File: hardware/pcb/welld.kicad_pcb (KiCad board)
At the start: 2 copper layers, 80 x 55 mm, 98 parts, among them J1 LiPo, J10 PROG, J12 Solar, J2 USB-C, J3 U.FL, J4 4-20mA_1, J5 4-20mA_2, J6 DS18B20, J7 Spare, J8 I2C, J9 GPIO, Q1 BSS123, Q2 BSS123, SW1 RESET, SW2 BOOT, U1 TPS7A0533, U10 MAX17048, U2 TP4056, U3 S-8261A, U4 FS8205A, U5 USBLC6, U6 ESP32-C6, U7 CN3791, U8 TPS61023, U9 ADS1115

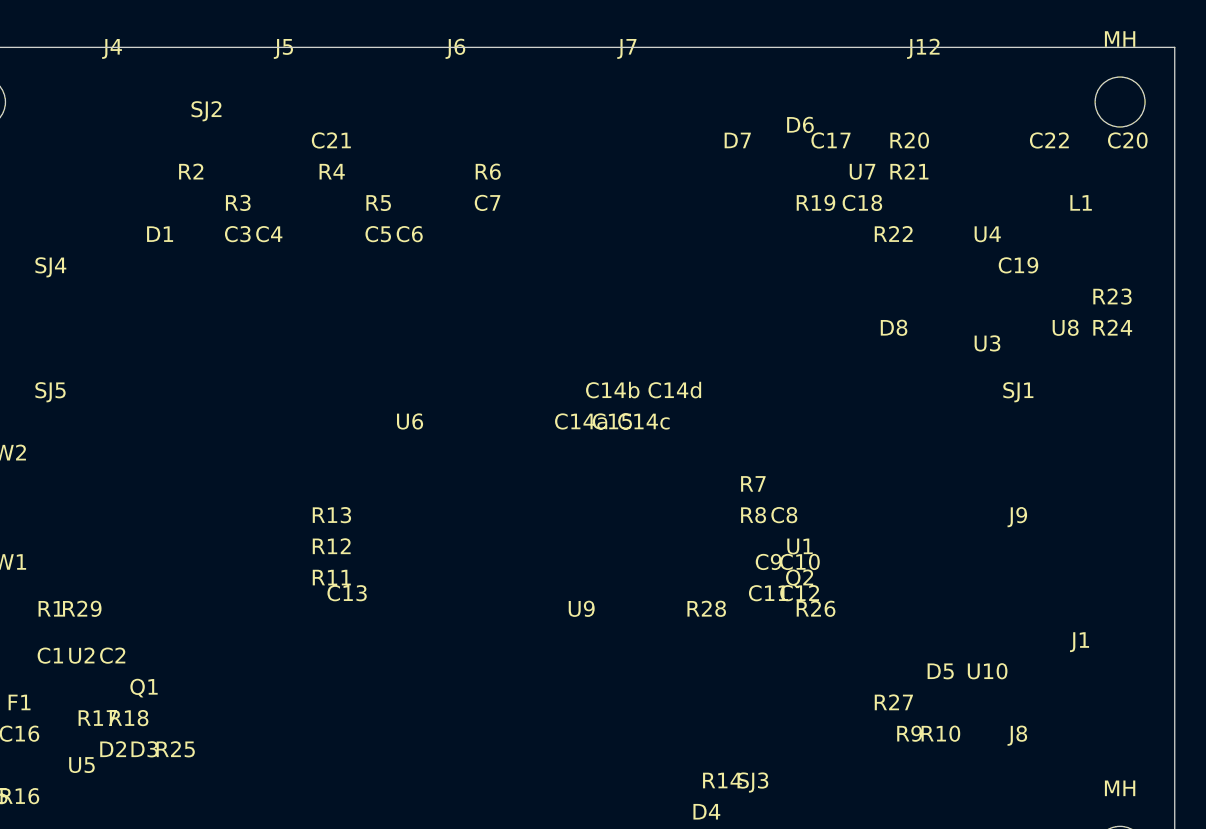
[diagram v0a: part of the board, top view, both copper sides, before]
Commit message: PCB analog/protection/interlock fixes + three new agents
Analog front-end:
- C3, C5: 100nF → 1µF to lower RC filter corner from 15.9kHz to 1.6kHz
- Add FB1 (BLM18KG601SN1D ferrite) + C23/C24 (ADS1115 VDD bypass) to isolate
  the 16-bit ADC supply from TPS61023 switching noise and 2.4GHz radio

Transient protection:
- Add D9/D10 (SMAJ5.0CA, bidirectional, 400W) at J4/J5 SIG terminals before
  the shunt resistors — IEC 61000-4-5 surge protection for well-head cables
- Add D11 (SMAJ13A, 13V standoff, 400W) on VLOOP rail between U8 and field
  terminals to clamp cable back-EMF and lightning-induced transients

Charger interlock:
- Fix GPIO6 polarity throughout: CN3791 CHRG is active-LOW (was documented
  as active-high in CLAUDE.md and design.md GPIO table)
- Fix design.md: CN3791 has no EN/shutdown pin; GPIO6 reads CHRG output only
- Add Q3 (BSS84 P-ch) hardware interlock: gate=/CHRG_SOLAR, source=CE node,
  drain=GND; eliminates the boot-window race without firmware involvement
- Add R30 (10kΩ) as Q3 gate pull-up to +3V3

Agents:
- Add test-engineer, docs-writer, ci-engineer agents to .claude/agents/
- Expand CLAUDE.md Sub-Agent Routing Rules with full responsibility table
  and handoff order for hardware vs firmware-only changes

Co-Authored-By: Claude Sonnet 4.6 <noreply@anthropic.com>
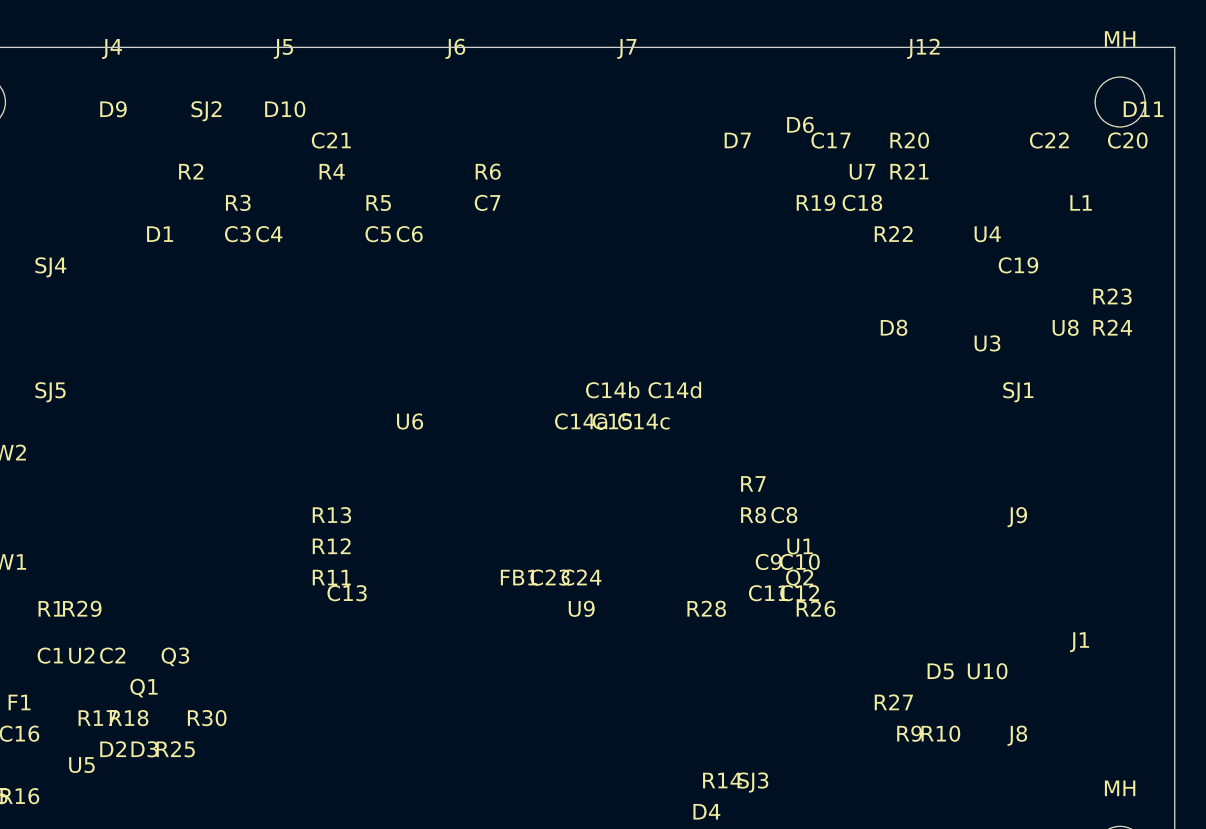
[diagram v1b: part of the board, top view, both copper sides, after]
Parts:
- added C23: 100nF, Capacitor_SMD:C_0402_1005Metric, F.Cu at (40.0, 36.0)
- added C24: 1uF, Capacitor_SMD:C_0402_1005Metric, F.Cu at (42.0, 36.0)
- added D10: SMAJ5.0CA, Diode_SMD:D_SMA, F.Cu at (23.0, 6.00)
- added D11: SMAJ13A, Diode_SMD:D_SMA, F.Cu at (78.0, 6.00)
- added D9: SMAJ5.0CA, Diode_SMD:D_SMA, F.Cu at (12.0, 6.00)
- added FB1: 600R@100MHz, Ferrite_Bead_SMD:L_0402_1005Metric, F.Cu at (38.0, 36.0)
- added Q3: BSS84, Package_TO_SOT_SMD:SOT-23, F.Cu at (16.0, 41.0)
- added R30: 10k, Resistor_SMD:R_0402_1005Metric, F.Cu at (18.0, 45.0)
- C3, C5: value 100nF -> 1uF
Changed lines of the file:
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@@
   (title_block
     (title "WellD Well-Level Monitor PCB")
-    (date "2026-05-16")
+    (date "2026-05-18")
     (company "WellD Project")
   )
@@
   (net 29 "ADS_DRDY")
   (net 30 "MAX_ALRT")
+  (net 31 "LOOP_TERM_CH1")
+  (net 32 "LOOP_TERM_CH2")
+  (net 33 "+3V3_ADS")
   (gr_line (start 0.000 0.000) (end 80.000 0.000)
     (stroke (width 0.05) (type solid)) (layer "Edge.Cuts")
@@
     )
   )
+  (footprint "Diode_SMD:D_SMA" (layer "F.Cu") (at 12.000 6.000 0.0)
+    (property "Reference" "D9" (at 0 -2 0) (layer "F.SilkS")
+      (effects (font (size 1 1) (thickness 0.15)))
+    )
+    (property "Value" "SMAJ5.0CA" (at 0 2 0) (layer "F.Fab")
+      (effects (font (size 1 1) (thickness 0.15)))
+    )
+  )
+  (footprint "Diode_SMD:D_SMA" (layer "F.Cu") (at 23.000 6.000 0.0)
+    (property "Reference" "D10" (at 0 -2 0) (layer "F.SilkS")
+      (effects (font (size 1 1) (thickness 0.15)))
+    )
+    (property "Value" "SMAJ5.0CA" (at 0 2 0) (layer "F.Fab")
+      (effects (font (size 1 1) (thickness 0.15)))
+    )
+  )
+  (footprint "Diode_SMD:D_SMA" (layer "F.Cu") (at 78.000 6.000 0.0)
+    (property "Reference" "D11" (at 0 -2 0) (layer "F.SilkS")
+      (effects (font (size 1 1) (thickness 0.15)))
+    )
+    (property "Value" "SMAJ13A" (at 0 2 0) (layer "F.Fab")
+      (effects (font (size 1 1) (thickness 0.15)))
+    )
+  )
   (footprint "LED_SMD:LED_0603_1608Metric" (layer "F.Cu") (at 12.000 47.000 0.0)
     (property "Reference" "D2" (at 0 -2 0) (layer "F.SilkS")
@@
       (effects (font (size 1 1) (thickness 0.15)))
     )
-    (property "Value" "100nF" (at 0 2 0) (layer "F.Fab")
+    (property "Value" "1uF" (at 0 2 0) (layer "F.Fab")
       (effects (font (size 1 1) (thickness 0.15)))
     )
@@
       (effects (font (size 1 1) (thickness 0.15)))
     )
-    (property "Value" "100nF" (at 0 2 0) (layer "F.Fab")
+    (property "Value" "1uF" (at 0 2 0) (layer "F.Fab")
       (effects (font (size 1 1) (thickness 0.15)))
     )
@@
     )
   )
+  (footprint "Ferrite_Bead_SMD:L_0402_1005Metric" (layer "F.Cu") (at 38.000 36.000 0.0)
+    (property "Reference" "FB1" (at 0 -2 0) (layer "F.SilkS")
+      (effects (font (size 1 1) (thickness 0.15)))
+    )
+    (property "Value" "600R@100MHz" (at 0 2 0) (layer "F.Fab")
+      (effects (font (size 1 1) (thickness 0.15)))
+    )
+  )
+  (footprint "Capacitor_SMD:C_0402_1005Metric" (layer "F.Cu") (at 40.000 36.000 0.0)
+    (property "Reference" "C23" (at 0 -2 0) (layer "F.SilkS")
+      (effects (font (size 1 1) (thickness 0.15)))
+    )
+    (property "Value" "100nF" (at 0 2 0) (layer "F.Fab")
+      (effects (font (size 1 1) (thickness 0.15)))
+    )
+  )
+  (footprint "Capacitor_SMD:C_0402_1005Metric" (layer "F.Cu") (at 42.000 36.000 0.0)
+    (property "Reference" "C24" (at 0 -2 0) (layer "F.SilkS")
+      (effects (font (size 1 1) (thickness 0.15)))
+    )
+    (property "Value" "1uF" (at 0 2 0) (layer "F.Fab")
+      (effects (font (size 1 1) (thickness 0.15)))
+    )
+  )
   (footprint "Package_SO:MSOP-10_3x3mm_P0.5mm" (layer "F.Cu") (at 42.000 38.000 0.0)
     (property "Reference" "U9" (at 0 -2 0) (layer "F.SilkS")
@@
     )
   )
+  (footprint "Package_TO_SOT_SMD:SOT-23" (layer "F.Cu") (at 16.000 41.000 0.0)
+    (property "Reference" "Q3" (at 0 -2 0) (layer "F.SilkS")
+      (effects (font (size 1 1) (thickness 0.15)))
+    )
+    (property "Value" "BSS84" (at 0 2 0) (layer "F.Fab")
+      (effects (font (size 1 1) (thickness 0.15)))
+    )
+  )
   (footprint "Resistor_SMD:R_0402_1005Metric" (layer "F.Cu") (at 16.000 47.000 0.0)
     (property "Reference" "R25" (at 0 -2 0) (layer "F.SilkS")
@@
       (effects (font (size 1 1) (thickness 0.15)))
     )
+  )
+  (footprint "Resistor_SMD:R_0402_1005Metric" (layer "F.Cu") (at 18.000 45.000 0.0)
+    (property "Reference" "R30" (at 0 -2 0) (layer "F.SilkS")
+      (effects (font (size 1 1) (thickness 0.15)))
+    )
+    (property "Value" "10k" (at 0 2 0) (layer "F.Fab")
+      (effects (font (size 1 1) (thickness 0.15)))
+    )

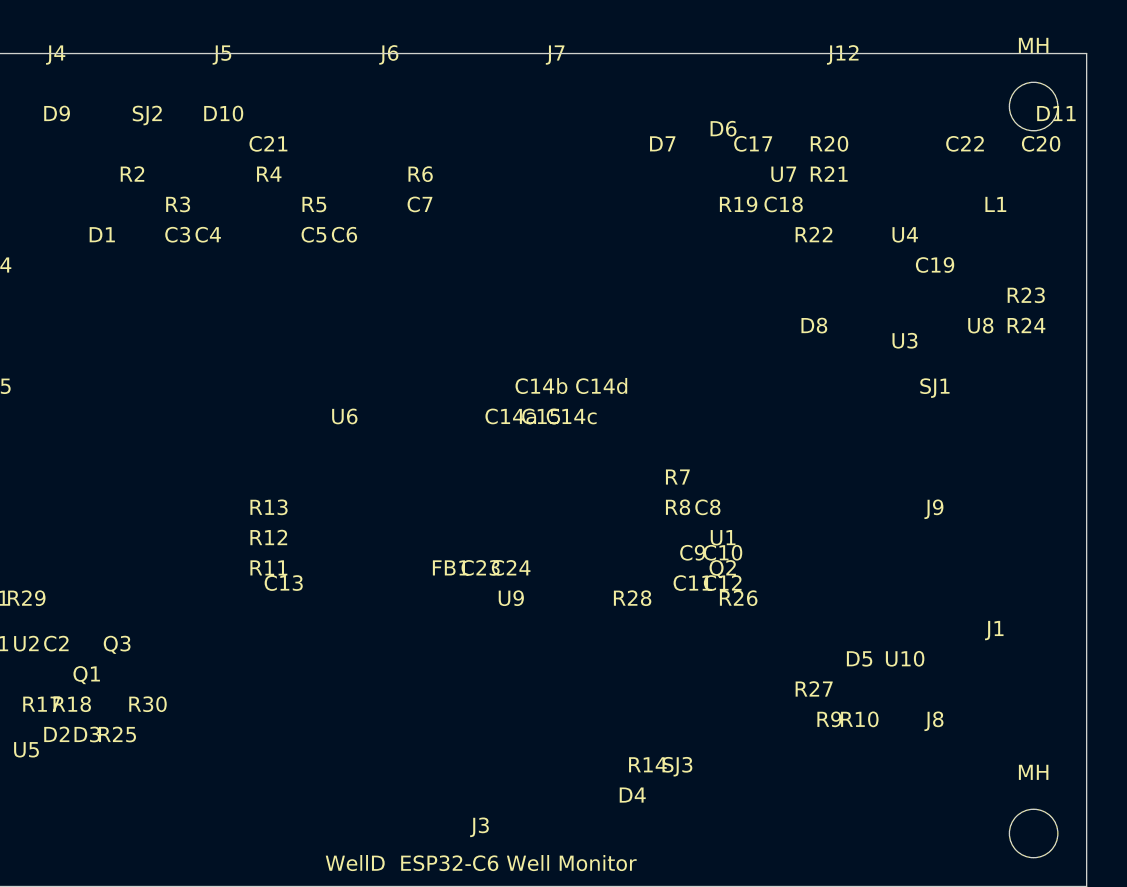
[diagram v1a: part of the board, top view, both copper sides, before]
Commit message: feat: PCB thermal/testpoints/decoupling, firmware robustness, Kconfig cleanup
PCB:
- CN3791 (U7): 10×10 mm GND thermal copper pour F.Cu+B.Cu with 4 thermal vias;
  handles 1.75 W worst-case simultaneous solar+boost load
- TPS61023 (U8): GND via-stitch ring around boost island for low-inductance return
- TP1–TP14: 1.0 mm SMD test points (DNF) for VBAT, VLOOP, 3V3, GND, LOOP+/-,
  SDA, SCL, 1WIRE, VSOLAR, VBAT_RAW, DRDY, ALRT, /CHRG
- C25, C26: 100 nF 0402 bypass caps on MAX17048 VDD and S-8261 VCC (previously missing)

Firmware:
- MAX17048 ALRT (GPIO14): startup level check + full STATUS flag decode
  (RI/VH/VL/VR/HD/SC) before clearing; replaces partial VL-only clear
- I2C bus recovery: 9-pulse SCL clock sequence on SDA-stuck detection at init
- Short-circuit detection: sensor_read_level() returns -2.0 for >21 mA loop current
- ADC oversampling (WELLD_ADC_OVERSAMPLE_ENABLED, default off): median-of-3 reads;
  opt-in for noisy installations
- Temperature compensation (WELLD_TEMP_COMPENSATION_ENABLED, default off):
  water-density correction at configurable ppm/°C
- DS18B20 resolution (WELLD_DS18B20_RESOLUTION_BITS, default 12-bit): saves up to
  656 ms/wakeup at 9-bit
- OTA rollback guard: RTC boot-attempt counter, rolls back partition after 3 fails
- Factory reset GPIO (WELLD_FACTORY_RESET_GPIO, default GPIO13): hold LOW at boot

Kconfig:
- Moved WELLD_ADC_OVERSAMPLE_ENABLED, WELLD_TEMP_COMPENSATION_*, WELLD_DS18B20_*,
  and WELLD_SOLAR_DETECT_GPIO from main/Kconfig.projbuild to components/sensor/Kconfig
  so standalone test/sensor build can see them; fixes CI on-device build failure

Co-Authored-By: Claude Sonnet 4.6 <noreply@anthropic.com>
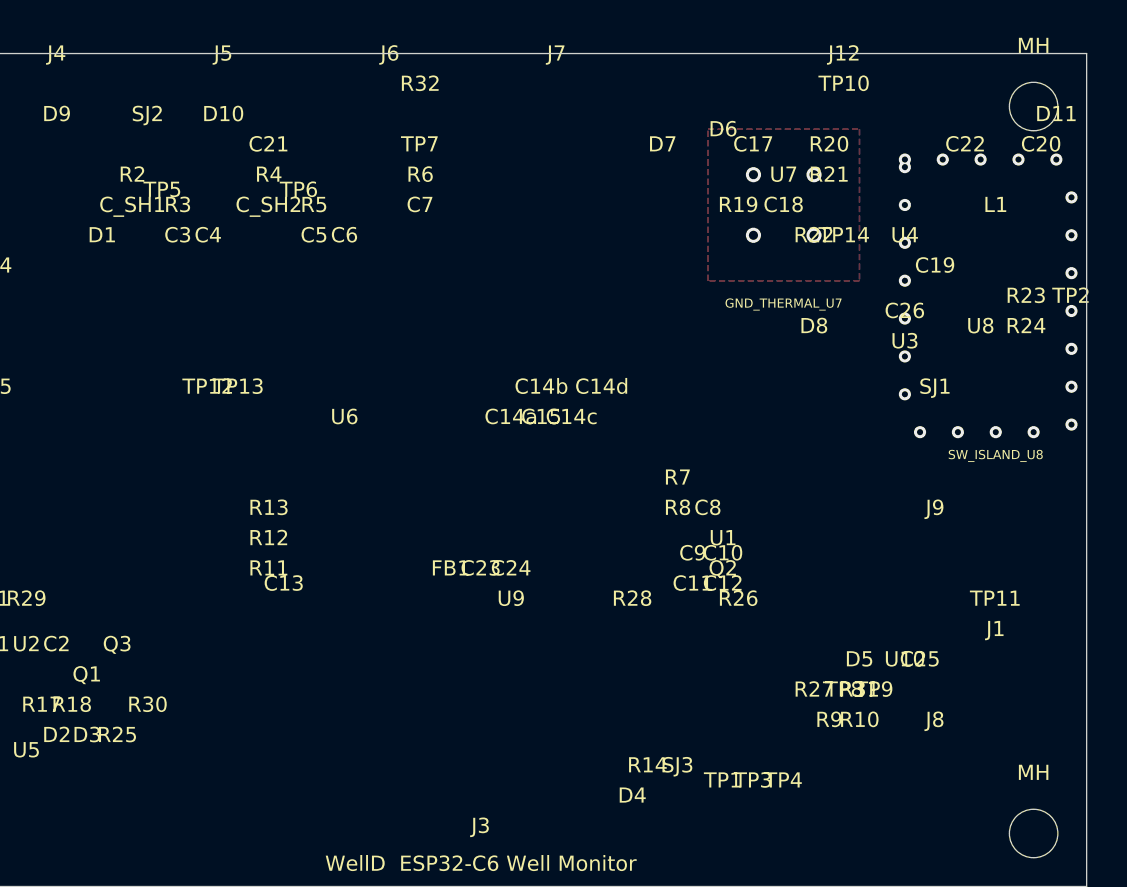
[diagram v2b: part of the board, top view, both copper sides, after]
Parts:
- added C25: 100nF, Capacitor_SMD:C_0402_1005Metric, F.Cu at (69.0, 42.0)
- added C26: 100nF, Capacitor_SMD:C_0402_1005Metric, F.Cu at (68.0, 19.0)
- added C_SH1: 10nF, Capacitor_SMD:C_0402_1005Metric, F.Cu at (17.0, 12.0)
- added C_SH2: 10nF, Capacitor_SMD:C_0402_1005Metric, F.Cu at (26.0, 12.0)
- added R31: 10k, Resistor_SMD:R_0402_1005Metric, F.Cu at (65.0, 44.0)
- added R32: 33R_DNF, Resistor_SMD:R_0402_1005Metric, F.Cu at (36.0, 4.00)
- added TP1: VBAT, TestPoint:TestPoint_Pad_1.0x1.0mm, F.Cu at (56.0, 50.0)
- added TP10: VSOLAR_IN, TestPoint:TestPoint_Pad_1.0x1.0mm, F.Cu at (64.0, 4.00)
- added TP11: VBAT_RAW, TestPoint:TestPoint_Pad_1.0x1.0mm, F.Cu at (74.0, 38.0)
- added TP12: ADS_DRDY, TestPoint:TestPoint_Pad_1.0x1.0mm, F.Cu at (22.0, 24.0)
- added TP13: MAX_ALRT, TestPoint:TestPoint_Pad_1.0x1.0mm, F.Cu at (24.0, 24.0)
- added TP14: /CHRG_SOLAR, TestPoint:TestPoint_Pad_1.0x1.0mm, F.Cu at (64.0, 14.0)
- added TP2: VLOOP, TestPoint:TestPoint_Pad_1.0x1.0mm, F.Cu at (79.0, 18.0)
- added TP3: +3V3, TestPoint:TestPoint_Pad_1.0x1.0mm, F.Cu at (58.0, 50.0)
- added TP4: GND, TestPoint:TestPoint_Pad_1.0x1.0mm, F.Cu at (60.0, 50.0)
- added TP5: LOOP_TERM_CH1, TestPoint:TestPoint_Pad_1.0x1.0mm, F.Cu at (19.0, 11.0)
- added TP6: LOOP_TERM_CH2, TestPoint:TestPoint_Pad_1.0x1.0mm, F.Cu at (28.0, 11.0)
- added TP7: 1WIRE, TestPoint:TestPoint_Pad_1.0x1.0mm, F.Cu at (36.0, 8.00)
- added TP8: I2C_SDA, TestPoint:TestPoint_Pad_1.0x1.0mm, F.Cu at (64.0, 44.0)
- added TP9: I2C_SCL, TestPoint:TestPoint_Pad_1.0x1.0mm, F.Cu at (66.0, 44.0)
- D10, D9: value SMAJ5.0CA -> SMAJ3.3CA
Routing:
- net GND: vias 0 -> 27
- added copper zone on B.Cu, net GND
- added copper zone on F.Cu, net GND
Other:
- board text added: "GND_THERMAL_U7"
- board text added: "SW_ISLAND_U8"

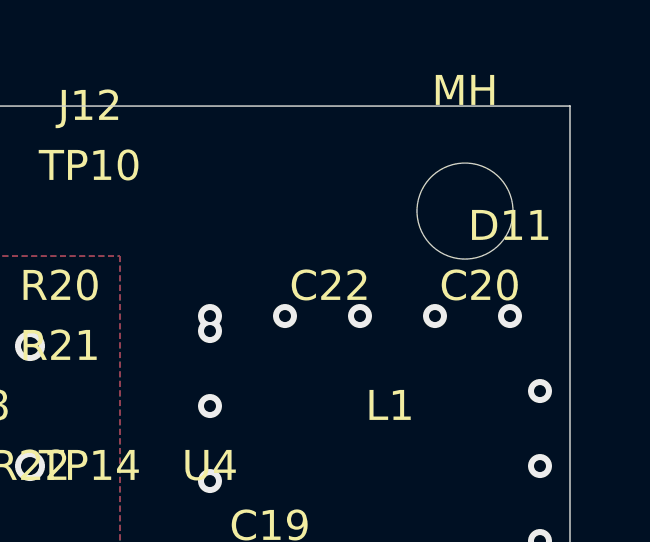
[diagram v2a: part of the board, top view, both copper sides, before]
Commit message: feat: 2S1P design — dual solar+USB-C charging, firmware, Z2M, PCB, case
Sinowatt 2S1P 18650 pack (6.0–8.4 V). Two independent charging paths:
- CN3722 MPPT solar charger via J12 screw terminal (GPIO6 /CHRG status)
- TP5100 USB-C boost charger via J13 connector (GPIO4 CE control)

PCB: AP63205 buck, MT3608B VLOOP boost, ADS1115 ADC, JST PH 2.0 mm battery
connector. SOC via resistor divider (BATT_DIVIDER_RATIO=430, FULL=8400 mV,
EMPTY=6000 mV). Firmware drives GPIO4 HIGH on wake to enable USB charging and
isolates it before deep-sleep so R37 passively holds CE LOW.

Case: battery bay 41×71×22 mm pocket for 2S1P pack; USB-C slot on left wall
for J13; programming gland repositioned to clear USB-C slot.

Z2M: 2S voltage thresholds and solar charge status reporting.

Tests: 2/2 host, 34/34 Z2M converter — all green.

Co-Authored-By: Claude Sonnet 4.6 <noreply@anthropic.com>
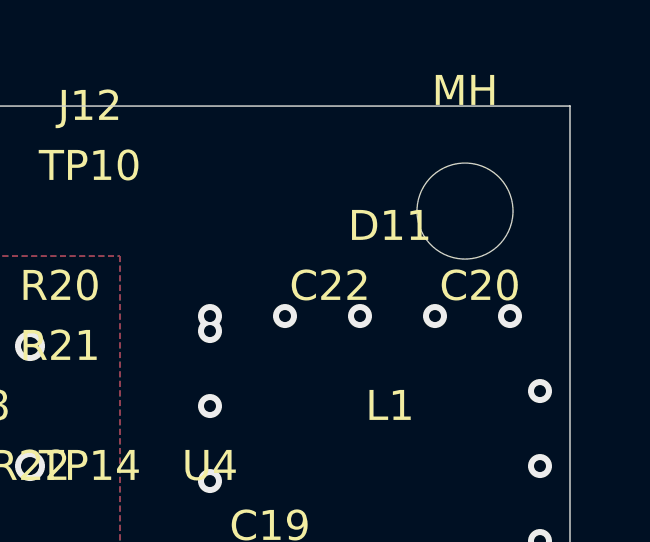
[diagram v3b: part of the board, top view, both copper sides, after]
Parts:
- moved D11 4.00 mm to (74.0, 6.00)
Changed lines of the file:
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@@
   (paper "A3")
   (title_block
-    (title "WellD Well-Level Monitor PCB")
+    (title "WellD Well-Level Monitor PCB — 2S 18650 LiPo")
     (date "2026-05-18")
     (company "WellD Project")
@@
   (net 2 "+3V3")
   (net 3 "VBAT")
-  (net 4 "VUSB")
-  (net 5 "VUSB_IN")
   (net 6 "VSOLAR")
   (net 7 "VSOLAR_IN")
@@
   (net 18 "BOOT")
   (net 19 "MPPT_REF")
-  (net 20 "/CHRG_USB")
-  (net 21 "/DONE_USB")
   (net 22 "/CHRG_SOLAR")
-  (net 23 "/DONE_SOLAR")
   (net 24 "VLOOP")
   (net 25 "VBOOST_EN")
-  (net 26 "CHRG_USB_DIS")
   (net 27 "SOLAR_DET")
   (net 28 "BATT_DIV_EN")
   (net 29 "ADS_DRDY")
-  (net 30 "MAX_ALRT")
   (net 31 "LOOP_TERM_CH1")
   (net 32 "LOOP_TERM_CH2")
@@
     )
   )
-  (footprint "Diode_SMD:D_SMA" (layer "F.Cu") (at 78.000 6.000 0.0)
+  (footprint "Diode_SMD:D_SMA" (layer "F.Cu") (at 74.000 6.000 0.0)
     (property "Reference" "D11" (at 0 -2 0) (layer "F.SilkS")
       (effects (font (size 1 1) (thickness 0.15)))
